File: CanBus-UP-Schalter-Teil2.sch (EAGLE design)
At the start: 28 parts, among them IC1 LM2937IMP-5.0, IC2 MEGA8-AI, IC3 MCP2515T-I/SO, Q1 EUROQUARTZ-MMJ, Q2 EUROQUARTZ-MMJ, Q3 BC847ASMD, Q4 BC847ASMD, U1 MCP2562-E/SN

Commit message: CanBus-UP-Schalter fertiggestellt
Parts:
- removed ISP1: ISPVIAS-ONLY-1.27MM, pogo-isp:ISPVIAS-ONLY-1.27MM
- added +5V, +5V1, PB0, PB1, PC4, PC5, PD7: LSP13, solpad:LSP13
- added ISP: ISPVIAS-ONLY-1.27MM, pogo-isp:ISPVIAS-ONLY-1.27MM
- added R5, R6: 4k7, rcl:R-EU_R0805
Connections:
- new net N$10: IC2.PC5(ADC5/SCL), PC5.MP, R6.1
- new net N$11: IC2.PC4(ADC4/SDA), PC4.MP, R5.1
- new net N$7: IC2.PB1(OC1A), PB1.MP
- new net N$8: IC2.PB0(ICP), PB0.MP
- new net N$9: IC2.PD7(AIN1), PD7.MP
- net +5V: now also +5V.MP, +5V1.MP, ISP.VCC, R5.2, R6.2; no longer ISP1.VCC
- net GND: now also ISP.GND; no longer ISP1.GND
- net MISO: now also ISP.MISO; no longer ISP1.MISO
- net MOSI: now also ISP.MOSI; no longer ISP1.MOSI
- net RST: now also ISP.RST; no longer ISP1.RST
- net SCK: now also ISP.SCK; no longer ISP1.SCK
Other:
- moved on the sheet: C1, C10, C11, C2, C3, C4, C5, C6, C7, C8, C9, IC1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

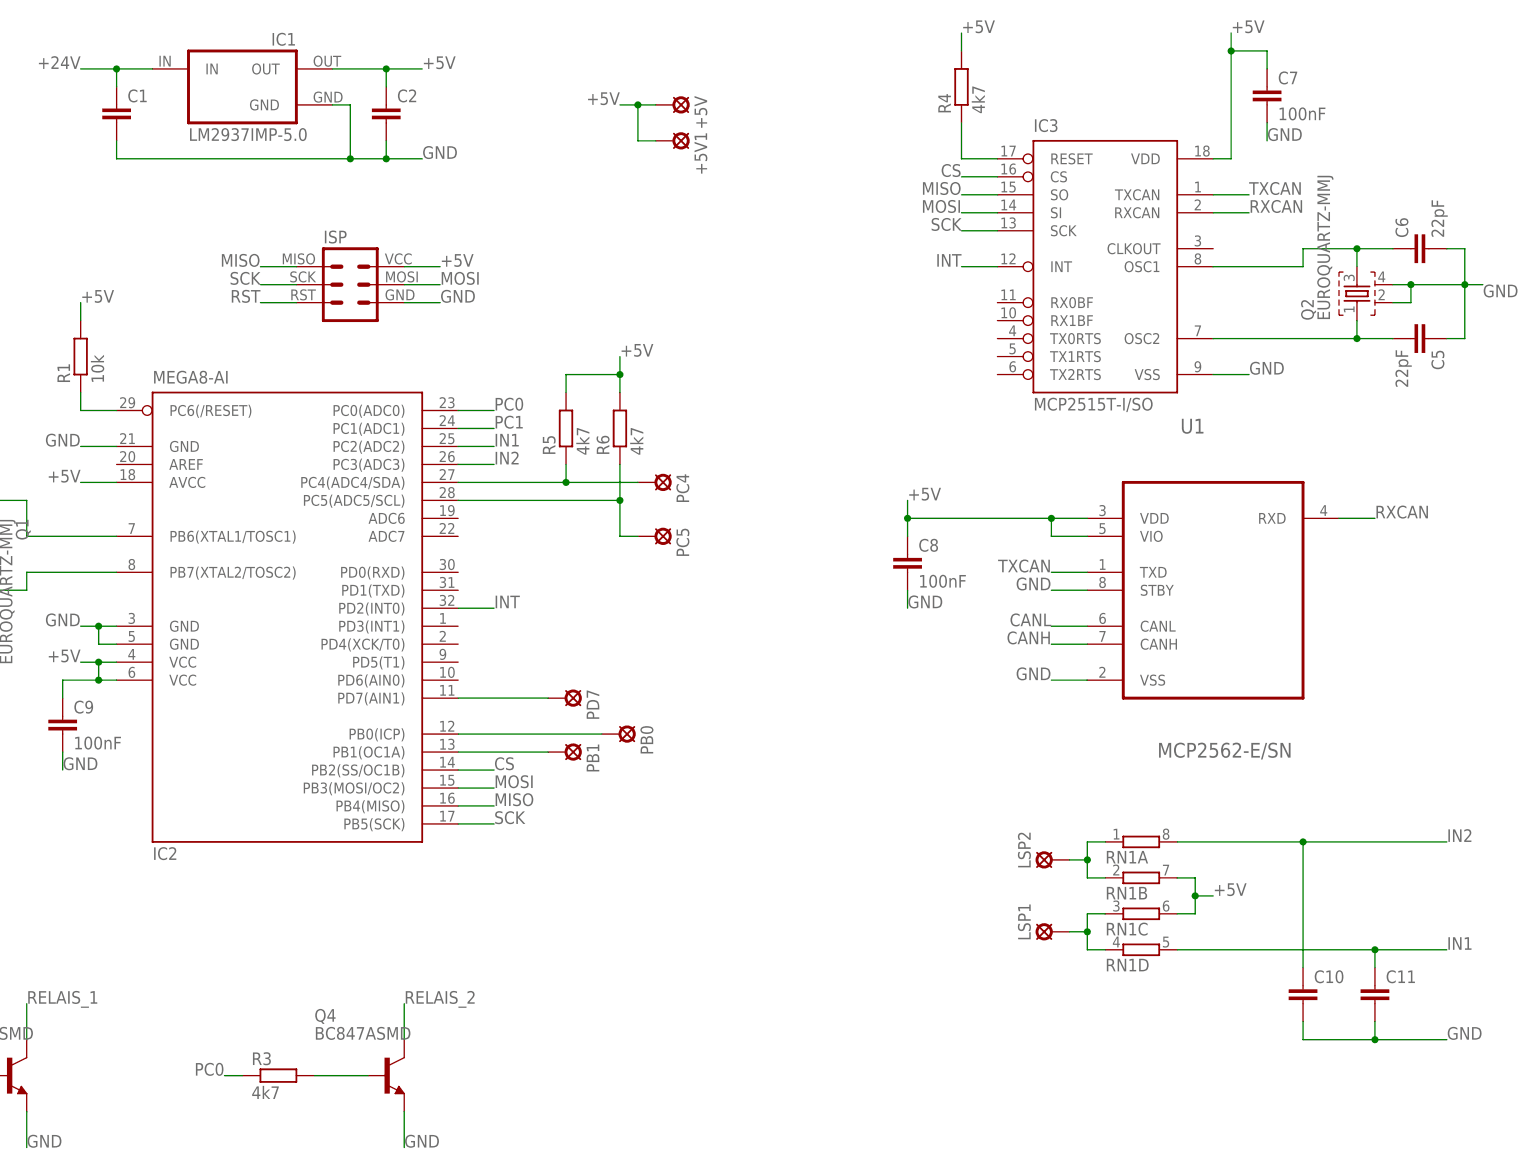
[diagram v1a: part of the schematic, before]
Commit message: Werte von Bauteilen angepasst
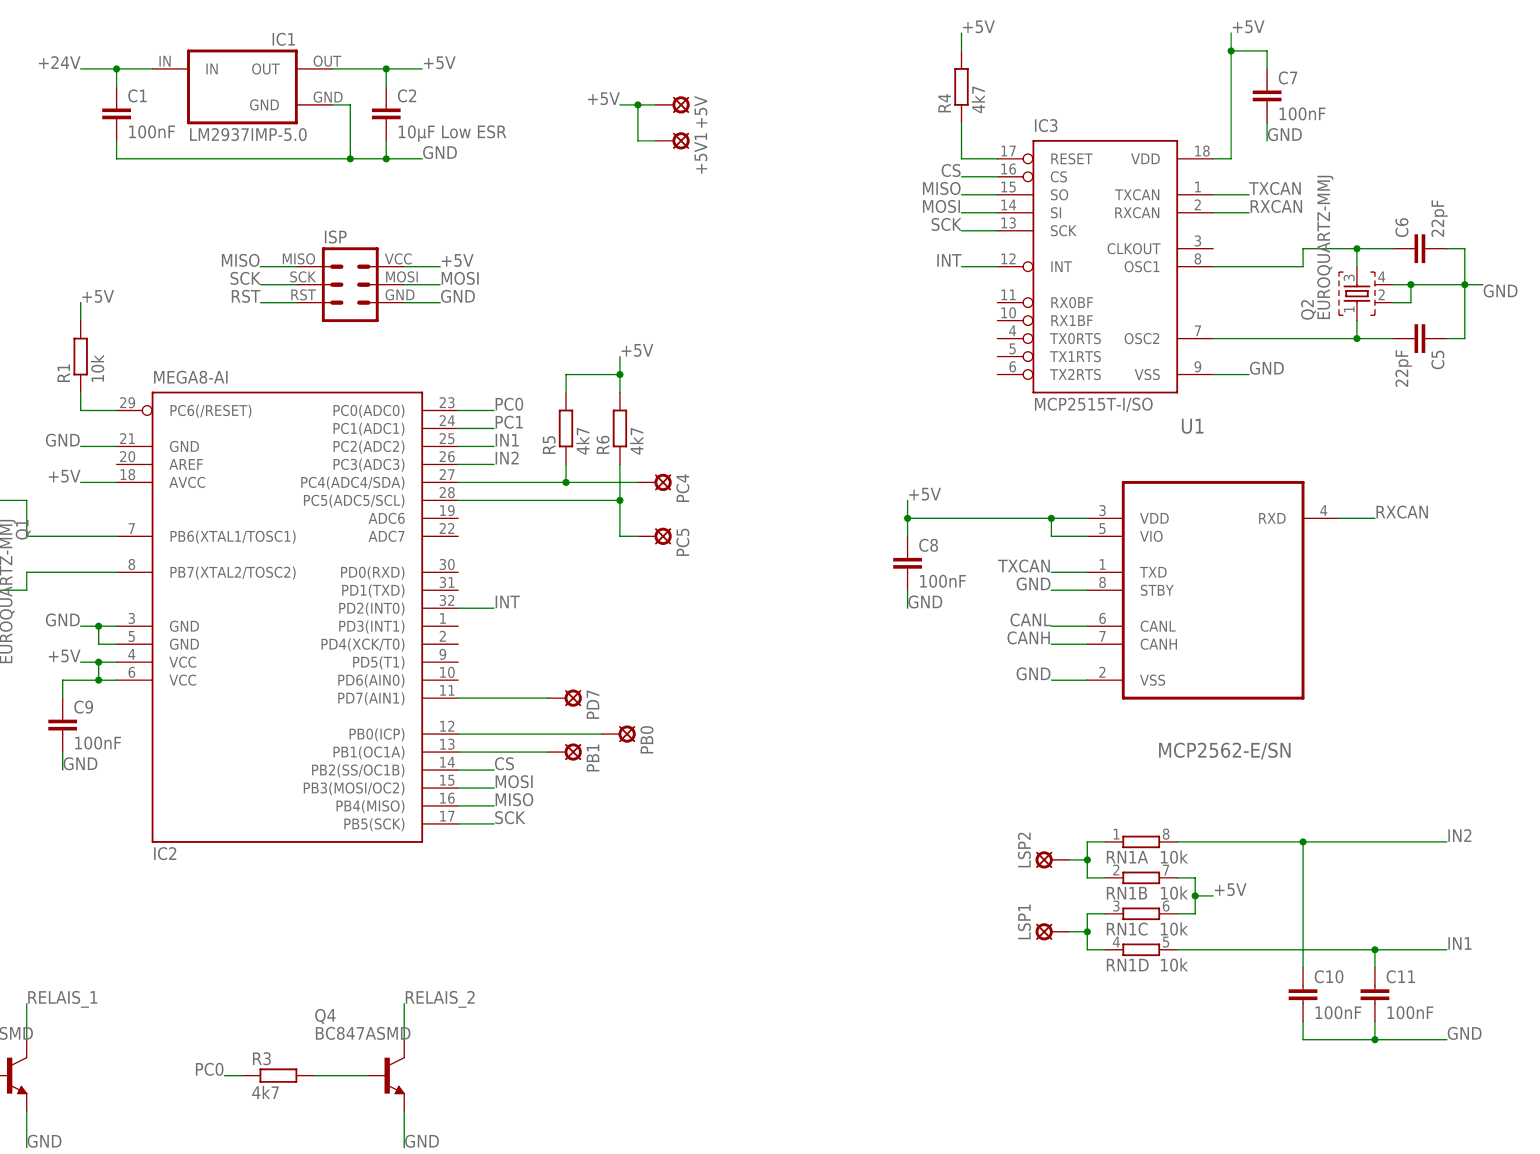
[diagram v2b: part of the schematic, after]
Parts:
- C1, C10, C11: value (none) -> 100nF
- C2: value (none) -> 10µF Low ESR
- RN1: value (none) -> 10k
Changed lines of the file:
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@@
 <parts>
 <part name="IC1" library="lm2937" deviceset="LM2937IMP-*" device="" technology="5.0"/>
-<part name="C1" library="rcl" deviceset="C-EU" device="C0805"/>
-<part name="C2" library="rcl" deviceset="C-EU" device="C0805"/>
+<part name="C1" library="rcl" deviceset="C-EU" device="C0805" value="100nF"/>
+<part name="C2" library="rcl" deviceset="C-EU" device="C0805" value="10µF Low ESR"/>
 <part name="SV1" library="con-lstb" deviceset="MA06-1" device=""/>
 <part name="IC2" library="atmel" deviceset="MEGA8" device="-AI"/>
@@
 <part name="C9" library="rcl" deviceset="C-EU" device="C0805" value="100nF"/>
 <part name="R4" library="rcl" deviceset="R-EU_" device="R0805" value="4k7"/>
-<part name="RN1" library="resistor-dil" deviceset="4R-N" device="0603-ARC"/>
-<part name="C10" library="rcl" deviceset="C-EU" device="C0805"/>
-<part name="C11" library="rcl" deviceset="C-EU" device="C0805"/>
+<part name="RN1" library="resistor-dil" deviceset="4R-N" device="0603-ARC" value="10k"/>
+<part name="C10" library="rcl" deviceset="C-EU" device="C0805" value="100nF"/>
+<part name="C11" library="rcl" deviceset="C-EU" device="C0805" value="100nF"/>
 <part name="LSP2" library="solpad" deviceset="LSP13" device=""/>
 <part name="LSP1" library="solpad" deviceset="LSP13" device=""/>
